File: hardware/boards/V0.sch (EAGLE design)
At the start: 141 parts, among them IC2 TPS6300, J12 3.5mm TRRS Jack, J2 HIROSE_DM3BT-DSF-PEJSHIROSE_D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, J3 MOLEX_105450-0101MOLEX_105450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, Q2 ON_SEMI_MMBT5551LT1GON_SEMI_M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, U1 VS1053-L, U2 MICROCHIP_MCP73831T-2ATI-OTMI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, X3 FH12-45S-0.5SH

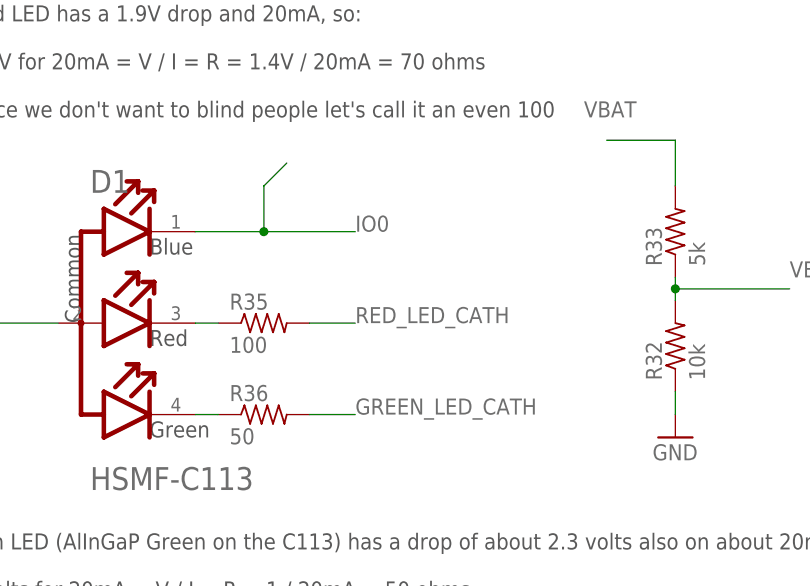
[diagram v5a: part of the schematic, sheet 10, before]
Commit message: Bridge IO0 and IO2 so that we can flash the board and use an SD Card
From the message on sheet 1:
IO2 is a strapping pin that allows the esp32 to enter download mode (iirc) - it's required to be pulled low when flashing the esp. Unforuntately, we have to use IO2 for the one usable SD/MMC interface on the esp32 (the other uses the same pins as flash).

IO0 is also a strapping pin: it's connected to RTS on the CP2102N and is pulled low when we're flashing the board. So, if we tie IO0 to IO2, IO2 will be pulled down while flashing. This solves our problem!

Unforunately this means that we can't use IO0 for anything else since it remains tied to IO2 (anything we do to IO0 will affect the SD/MMC peripheral). We could use a fancy circuit that pulls IO2 low only when the chip is reset (for a second or so) or do some transistor magic (only pull IO2 low when multiple other pins are low or something), but since we're only using IO0 for an LED, I figure it's not worth the trouble.

We'll move the LED's net to something else and connect IO0 and IO2.

Ended up putting the green and blue LEDs on the same pin. Since the voltage drops are different, hopefully we can get slightly different colors by PWMing at different frequencies.
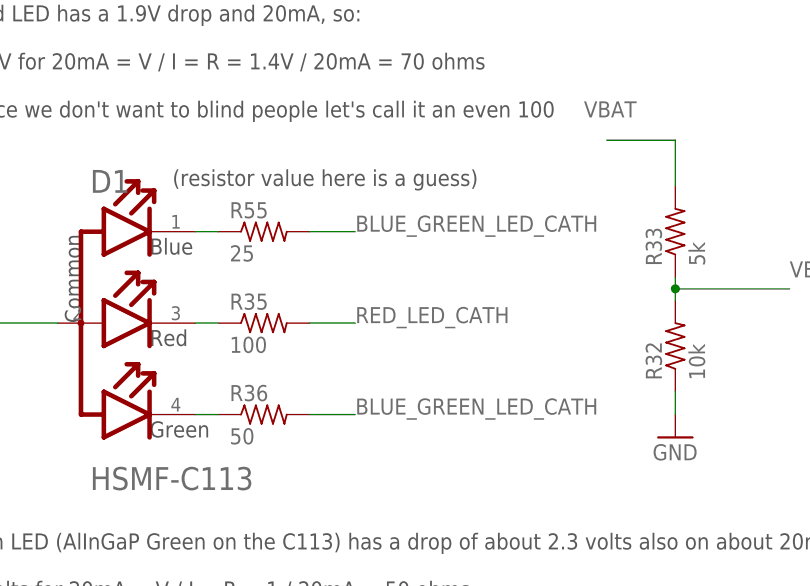
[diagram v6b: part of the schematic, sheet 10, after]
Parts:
- added R55: 25, rcl:R-US_R0402
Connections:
- removed net GREEN_LED_CATH: R36.2, U$1.IO9
- new net BLUE_GREEN_LED_CATH: R36.2, R55.2, U$1.IO9
- new net N$2: D1.BLUE_CATHODE, R55.1
- net IO0: no longer D1.BLUE_CATHODE, U$1.IO0
- net IO2: now also U$1.IO0
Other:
- note added: "(resistor value here is a guess)"
- note added: "IO2 is a strapping pin that allows the esp32 to enter download mode (iirc) - it's required to be pulled low when flashing the esp. Unforuntately, we have to use IO2 for the one usable SD/MMC interface on the esp32 (the other uses the same pins as flash). IO0 is also a strapping pin: it's connected to RTS on the CP2102N and is pulled low when we're flashing the board. So, if we tie IO0 to IO2, IO2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"
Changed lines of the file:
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@@
 <part name="R53" library="rcl" library_urn="urn:adsk.eagle:library:334" deviceset="R-US_" device="R0805" package3d_urn="urn:adsk.eagle:package:23553/2" value="10k"/>
 <part name="R54" library="rcl" library_urn="urn:adsk.eagle:library:334" deviceset="R-US_" device="R0805" package3d_urn="urn:adsk.eagle:package:23553/2" value="315k"/>
+<part name="R55" library="rcl" library_urn="urn:adsk.eagle:library:334" deviceset="R-US_" device="R0402" package3d_urn="urn:adsk.eagle:package:23547/3" value="25"/>
 </parts>
 <sheets>
@@
 indeed disconnected as shown on the esp32 pico dev board
 schematic (NC) and on this: https://cdn.hackaday.io/files/853893653282976/ESP32-Prog-1.pdf</text>
+<text x="66.04" y="-111.76" size="1.778" layer="97">IO2 is a strapping pin that allows the esp32 to enter download
+mode (iirc) - it's required to be pulled low when flashing the esp.
+Unforuntately, we have to use IO2 for the one usable SD/MMC
+interface on the esp32 (the other uses the same pins as flash).
+IO0 is also a strapping pin: it's connected to RTS on the CP2102N
+and is pulled low when we're flashing the board. So, if we tie IO0
+to IO2, IO2 will be pulled down while flashing. This solves our
+problem!
+Unforunately this means that we can't use IO0 for anything else
+since it remains tied to IO2 (anything we do to IO0 will affect the
+SD/MMC peripheral). We could use a fancy circuit that pulls IO2
+low only when the chip is reset (for a second or so) or do some
+transistor magic (only pull IO2 low when multiple other pins are
+low or something), but since we're only using IO0 for an LED, I
+figure it's not worth the trouble.
+We'll move the LED's net to something else and connect IO0 and
+IO2.</text>
 </plain>
 <instances>
@@
 <label x="-68.58" y="-93.98" size="1.778" layer="95"/>
 </segment>
-<segment>
-<pinref part="U$1" gate="G$1" pin="IO0"/>
-<wire x1="22.86" y1="-50.8" x2="22.86" y2="-68.58" width="0.1524" layer="91"/>
-<label x="22.86" y="-71.12" size="1.778" layer="95" rot="R270"/>
-</segment>
 </net>
 <net name="V3P3" class="0">
@@
 <wire x1="17.78" y1="-50.8" x2="17.78" y2="-68.58" width="0.1524" layer="91"/>
 <label x="17.78" y="-71.12" size="1.778" layer="95" rot="R270"/>
+<pinref part="U$1" gate="G$1" pin="IO0"/>
+<wire x1="22.86" y1="-50.8" x2="22.86" y2="-68.58" width="0.1524" layer="91"/>
+<wire x1="17.78" y1="-68.58" x2="22.86" y2="-68.58" width="0.1524" layer="91"/>
 </segment>
 </net>
@@
 </segment>
 </net>
-<net name="GREEN_LED_CATH" class="0">
+<net name="BLUE_GREEN_LED_CATH" class="0">
 <segment>
 <pinref part="U$1" gate="G$1" pin="IO9"/>
@@
 <text x="106.68" y="12.7" size="1.778" layer="97">I'm not sure this will work, so leave this resistor
 off initially/until we've thought it through.</text>
+<text x="-12.7" y="15.24" size="1.778" layer="97">(resistor value here is a guess)</text>
 </plain>
 <instances>
@@
 <attribute name="VALUE" x="102.362" y="11.43" size="1.778" layer="96" rot="R90"/>
 </instance>
+<instance part="R55" gate="G$1" x="-2.54" y="10.16" smashed="yes">
+<attribute name="NAME" x="-6.35" y="11.6586" size="1.778" layer="95"/>
+<attribute name="VALUE" x="-6.35" y="6.858" size="1.778" layer="96"/>
+</instance>
 </instances>
 <busses>
@@
 </segment>
 </net>
-<net name="GREEN_LED_CATH" class="0">
-<segment>
-<pinref part="R36" gate="G$1" pin="2"/>
-<wire x1="2.54" y1="-10.16" x2="7.62" y2="-10.16" width="0.1524" layer="91"/>
-<label x="7.62" y="-10.16" size="1.778" layer="95"/>
-</segment>
-</net>
-<net name="IO0" class="0">
-<segment>
-<pinref part="D1" gate="G$0" pin="BLUE_CATHODE"/>
-<wire x1="-10.16" y1="10.16" x2="-2.54" y2="10.16" width="0.1524" layer="91"/>
-<label x="7.62" y="10.16" size="1.778" layer="95"/>
-<wire x1="-2.54" y1="10.16" x2="7.62" y2="10.16" width="0.1524" layer="91"/>
-<wire x1="-2.54" y1="10.16" x2="-2.54" y2="15.24" width="0.1524" layer="91"/>
-<wire x1="-2.54" y1="15.24" x2="0" y2="17.78" width="0.1524" layer="91"/>
-<junction x="-2.54" y="10.16"/>
-</segment>
-</net>
 <net name="TRRS_INLINE_CTRL" class="0">
 <segment>
@@
 </segment>
 </net>
+<net name="N$2" class="0">
+<segment>
+<pinref part="D1" gate="G$0" pin="BLUE_CATHODE"/>
+<pinref part="R55" gate="G$1" pin="1"/>
+<wire x1="-10.16" y1="10.16" x2="-7.62" y2="10.16" width="0.1524" layer="91"/>
+</segment>
+</net>
+<net name="BLUE_GREEN_LED_CATH" class="0">
+<segment>
+<pinref part="R55" gate="G$1" pin="2"/>
+<wire x1="2.54" y1="10.16" x2="7.62" y2="10.16" width="0.1524" layer="91"/>
+<label x="7.62" y="10.16" size="1.778" layer="95"/>
+</segment>
+<segment>
+<pinref part="R36" gate="G$1" pin="2"/>
+<wire x1="2.54" y1="-10.16" x2="7.62" y2="-10.16" width="0.1524" layer="91"/>
+<label x="7.62" y="-10.16" size="1.778" layer="95"/>
+</segment>
+</net>

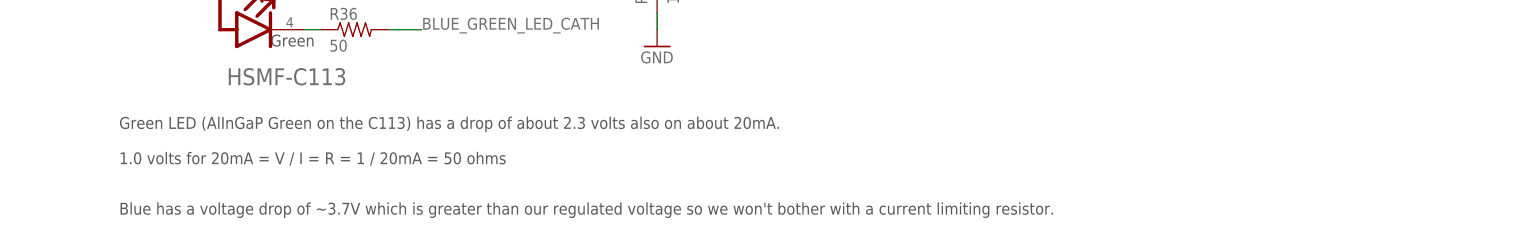
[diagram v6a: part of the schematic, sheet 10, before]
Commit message: magnet positions: a guess
the BOM is updated now too; gonna go with [these magnets](https://www.ebay.com/itm/1-100-Rare-Earth-Magnets-Neodymium-Round-Disk-Super-Strong-Large-Sizes-USA/122945482155), probably

this closes #14
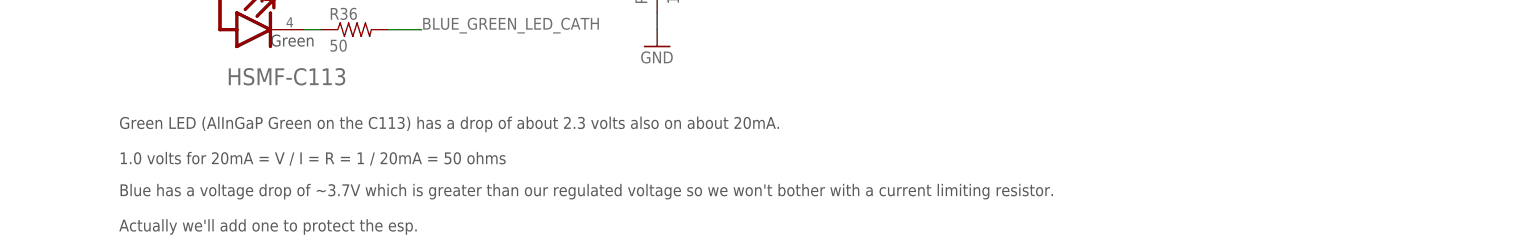
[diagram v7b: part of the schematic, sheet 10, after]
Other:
- note added: "Blue has a voltage drop of ~3.7V which is greater than our regulated voltage so we won't bother with a current limiting resistor. Actually we'll add one to protect the esp."
- note removed: "Blue has a voltage drop of ~3.7V which is greater than our regulated voltage so we won't bother with a current limiting resistor."
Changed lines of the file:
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@@
 <text x="-38.1" y="-30.48" size="1.778" layer="97">Green LED (AlInGaP Green on the C113) has a drop of about 2.3 volts also on about 20mA.
 1.0 volts for 20mA = V / I = R = 1 / 20mA = 50 ohms</text>
-<text x="-38.1" y="-38.1" size="1.778" layer="97">Blue has a voltage drop of ~3.7V which is greater than our regulated voltage so we won't bother with a current limiting resistor.</text>
+<text x="-38.1" y="-40.64" size="1.778" layer="97">Blue has a voltage drop of ~3.7V which is greater than our regulated voltage so we won't bother with a current limiting resistor.
+Actually we'll add one to protect the esp.</text>
 <text x="106.68" y="12.7" size="1.778" layer="97">I'm not sure this will work, so leave this resistor
 off initially/until we've thought it through.</text>

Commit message: checkpoint: 3.3V regulator
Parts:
- added C37: 10uF, rcl:C-USC0402
- C2, C3: device rcl:C-USC0603 -> rcl:C-USC0402
- C26, C27, C35: device rcl:C-USC0805 -> rcl:C-USC0402
- C4: value 4.7 uF -> 10uF; device rcl:C-USC0805 -> rcl:C-USC0402
- C5: device rcl:C-USC1210 -> rcl:C-USC0402
- R3, R34, R51, R52: device rcl:R-US_R0805 -> rcl:R-US_R0402
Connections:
- net GND: now also C37.2, IC2TH.TH
- net V3P3: now also C37.1
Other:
- moved on the sheet: TP1
